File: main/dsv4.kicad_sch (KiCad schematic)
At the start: 2 parts, among them J101 Conn_01x02, J102 Conn_01x02

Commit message: Update, with FTDI, mostly OK
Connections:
- no-connect marks 0 -> 6
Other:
- added sheet MOT B Connection (mot_connector.kicad_sch)
- sheet MCU ports: added SPI_~{CS}_1, SPI_~{CS}_2, USART{UART}; removed none
- sheet MOT A Connection ports: added COD_PWM, COD_U, COD_V, COD{ENC}, MOT{MOT}, SPI_CSN, SPI{SPI}; removed none
- sheet Radio and misc ports: added UART{UART}; removed none

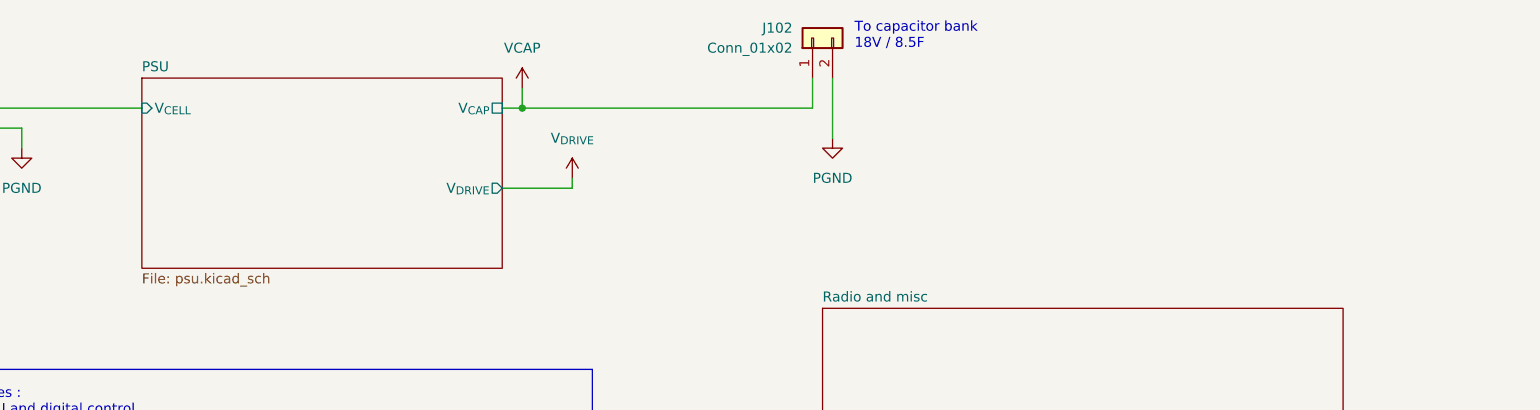
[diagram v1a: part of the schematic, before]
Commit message: Finalize schema for bat charger
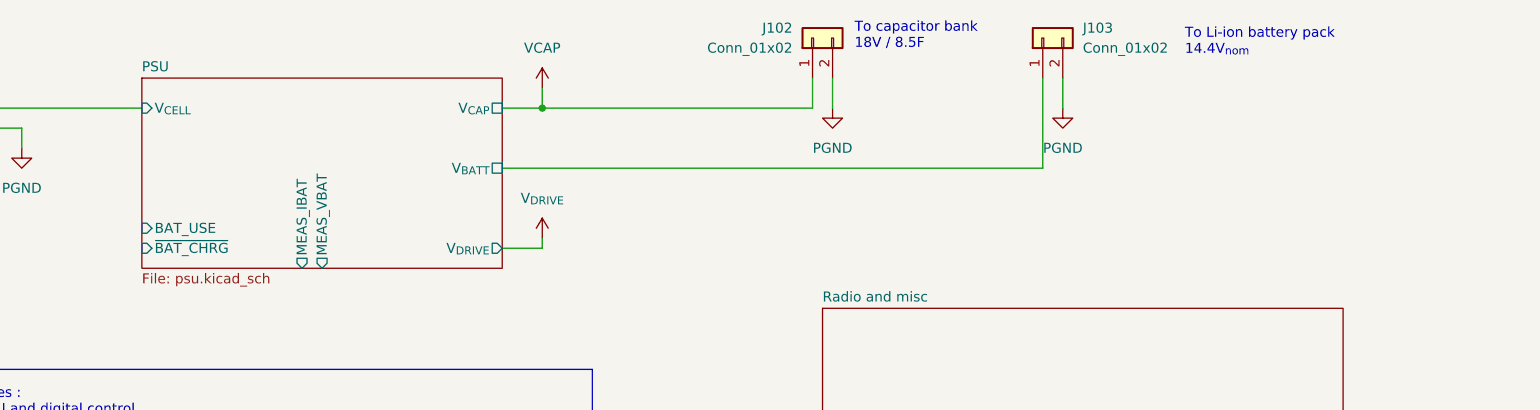
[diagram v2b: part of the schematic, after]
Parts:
- added J103: Conn_01x02, symbol Connector_Generic:Conn_01x02
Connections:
- net PGND: now also J103.2 (Pin_2)
- new net PSU/V_{BATT}: J103.1 (Pin_1)
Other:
- sheet PSU ports: added BAT_USE, MEAS_IBAT, MEAS_VBAT, V_{BATT}, ~{BAT_CHRG}; removed none
- note added: "To Li-ion battery pack 14.4V_{nom}"

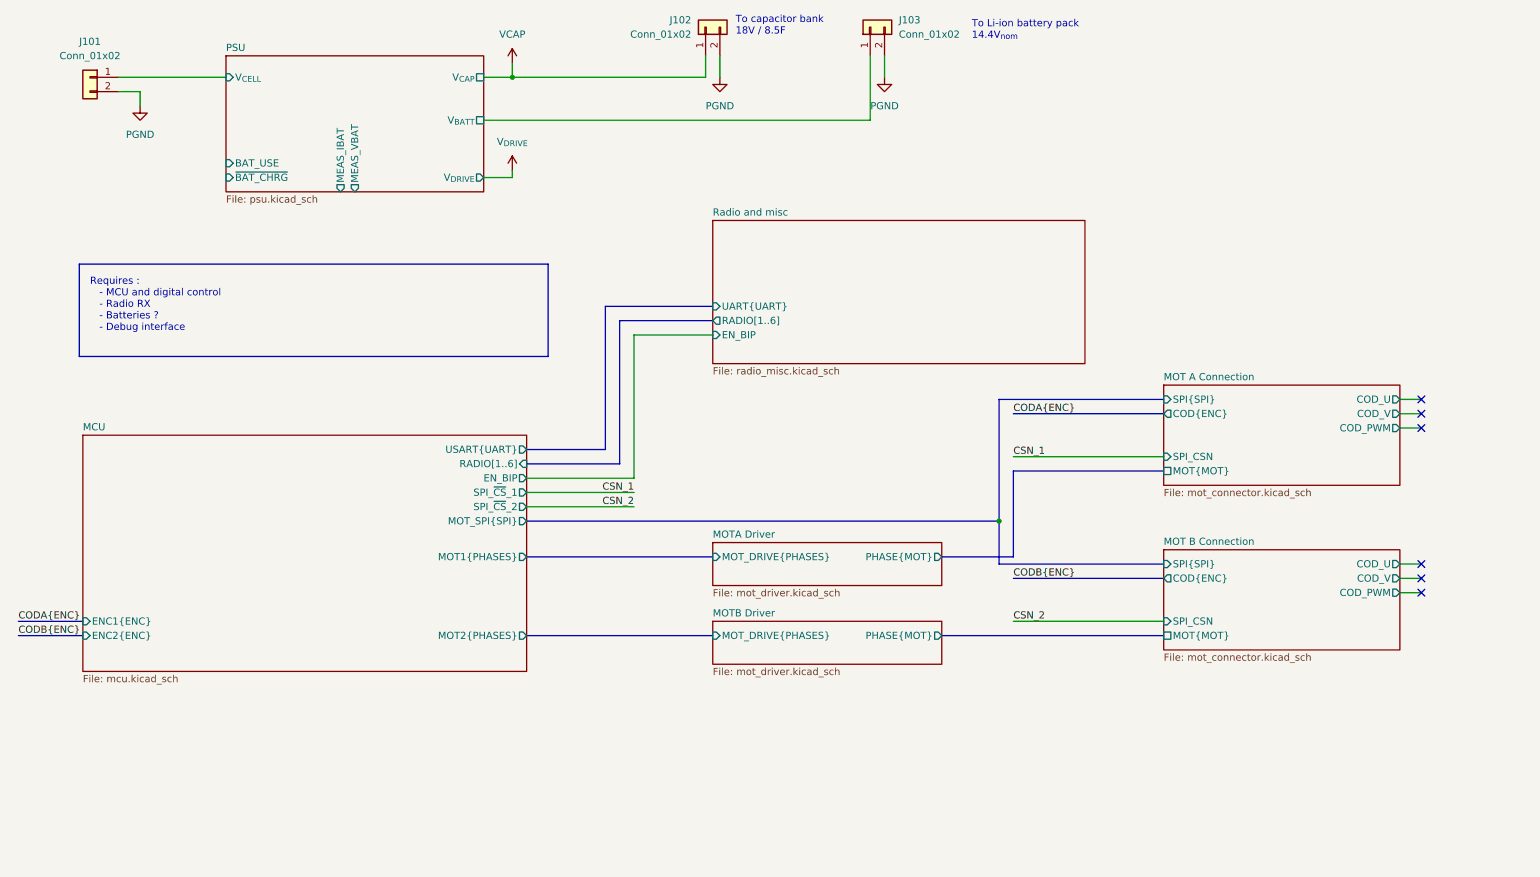
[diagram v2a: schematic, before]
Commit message: Finalize sch and start component mapping
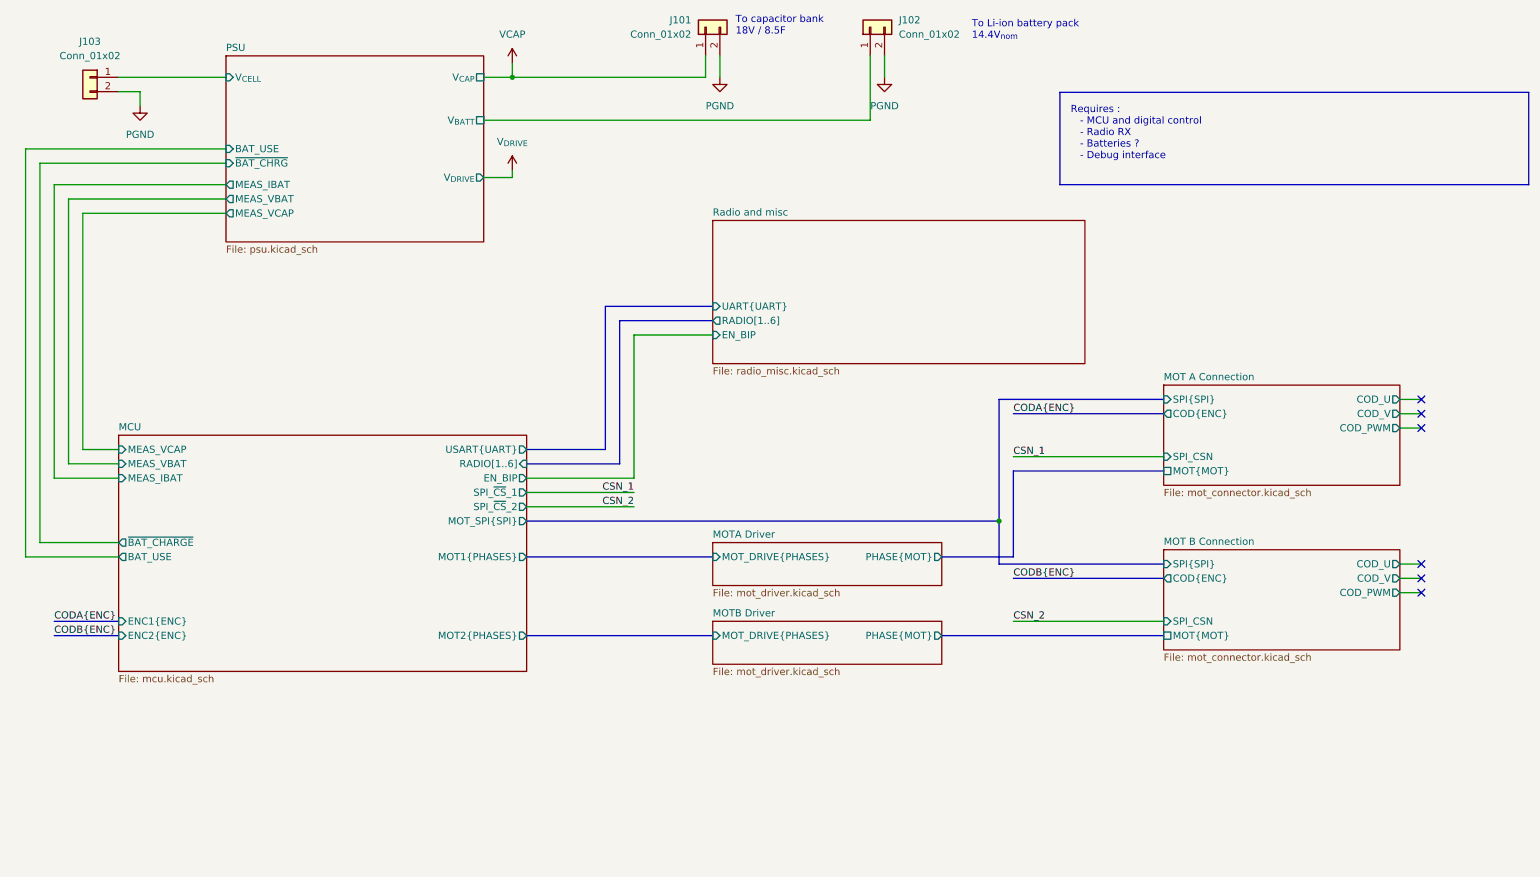
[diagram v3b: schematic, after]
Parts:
- renumbered J102 to J101, J103 to J102, J101 to J103
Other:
- sheet MCU ports: added BAT_USE, MEAS_IBAT, MEAS_VBAT, MEAS_VCAP, ~{BAT_CHARGE}; removed none
- sheet PSU ports: added MEAS_VCAP; removed none
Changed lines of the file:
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@@
+	(wire
+		(pts
+			(xy 17.78 110.49) (xy 17.78 43.18)
+		)
+		(stroke
+			(width 0)
+			(type default)
+		)
+	)
 	(wire
 		(pts
@@
 		)
 	)
+	(wire
+		(pts
+			(xy 25.4 93.98) (xy 25.4 52.07)
+		)
+		(stroke
+			(width 0)
+			(type default)
+		)
+	)
 	(bus
 		(pts
@@
 	(bus
 		(pts
-			(xy 13.97 127) (xy 25.4 127)
+			(xy 20.32 127) (xy 31.75 127)
 		)
 		(stroke
@@
 	(wire
 		(pts
+			(xy 17.78 43.18) (xy 50.8 43.18)
+		)
+		(stroke
+			(width 0)
+			(type default)
+		)
+	)
+	(wire
+		(pts
 			(xy 96.52 27.94) (xy 101.6 27.94)
 		)
@@
 	(wire
 		(pts
+			(xy 15.24 40.64) (xy 15.24 113.03)
+		)
+		(stroke
+			(width 0)
+			(type default)
+		)
+	)
+	(wire
+		(pts
 			(xy 190.5 124.46) (xy 217.17 124.46)
 		)
@@
 		)
 	)
+	(wire
+		(pts
+			(xy 20.32 46.99) (xy 20.32 99.06)
+		)
+		(stroke
+			(width 0)
+			(type default)
+		)
+	)
 	(bus
 		(pts
@@
 	(bus
 		(pts
-			(xy 13.97 124.46) (xy 25.4 124.46)
+			(xy 20.32 124.46) (xy 31.75 124.46)
 		)
 		(stroke
@@
 	(wire
 		(pts
+			(xy 50.8 46.99) (xy 20.32 46.99)
+		)
+		(stroke
+			(width 0)
+			(type default)
+		)
+	)
+	(wire
+		(pts
 			(xy 104.14 104.14) (xy 123.19 104.14)
 		)
@@
 	(wire
 		(pts
+			(xy 22.86 49.53) (xy 22.86 96.52)
+		)
+		(stroke
+			(width 0)
+			(type default)
+		)
+	)
+	(wire
+		(pts
 			(xy 123.19 99.06) (xy 104.14 99.06)
 		)
@@
 		)
 	)
+	(wire
+		(pts
+			(xy 50.8 40.64) (xy 15.24 40.64)
+		)
+		(stroke
+			(width 0)
+			(type default)
+		)
+	)
 	(bus
 		(pts
@@
 	(wire
 		(pts
+			(xy 50.8 49.53) (xy 22.86 49.53)
+		)
+		(stroke
+			(width 0)
+			(type default)
+		)
+	)
+	(wire
+		(pts
 			(xy 96.52 35.56) (xy 165.1 35.56)
 		)
@@
 		)
 	)
+	(wire
+		(pts
+			(xy 15.24 113.03) (xy 31.75 113.03)
+		)
+		(stroke
+			(width 0)
+			(type default)
+		)
+	)
+	(wire
+		(pts
+			(xy 31.75 93.98) (xy 25.4 93.98)
+		)
+		(stroke
+			(width 0)
+			(type default)
+		)
+	)
+	(wire
+		(pts
+			(xy 20.32 99.06) (xy 31.75 99.06)
+		)
+		(stroke
+			(width 0)
+			(type default)
+		)
+	)
 	(bus
 		(pts
@@
 		)
 	)
+	(wire
+		(pts
+			(xy 31.75 110.49) (xy 17.78 110.49)
+		)
+		(stroke
+			(width 0)
+			(type default)
+		)
+	)
 	(bus
 		(pts
@@
 	(wire
 		(pts
+			(xy 22.86 96.52) (xy 31.75 96.52)
+		)
+		(stroke
+			(width 0)
+			(type default)
+		)
+	)
+	(wire
+		(pts
 			(xy 167.64 24.13) (xy 167.64 27.94)
 		)
@@
 		)
 	)
+	(wire
+		(pts
+			(xy 25.4 52.07) (xy 50.8 52.07)
+		)
+		(stroke
+			(width 0)
+			(type default)
+		)
+	)
 	(rectangle
-		(start 24.765 61.087)
-		(end 107.95 77.47)
+		(start 198.755 30.607)
+		(end 281.94 46.99)
 		(stroke
 			(width 0)
@@
 	(text "Requires :\n   - MCU and digital control\n   - Radio RX\n   - Batteries ?\n   - Debug interface"
 		(exclude_from_sim no)
-		(at 26.67 63.5 0)
+		(at 200.66 33.02 0)
 		(effects
 			(font
@@
 	)
 	(label "CODB{ENC}"
-		(at 13.97 127 0)
+		(at 20.32 127 0)
 		(fields_autoplaced yes)
 		(effects
@@
 	)
 	(label "CODA{ENC}"
-		(at 13.97 124.46 0)
+		(at 20.32 124.46 0)
 		(fields_autoplaced yes)
 		(effects
@@
 		(dnp no)
 		(fields_autoplaced yes)
-		(property "Reference" "#PWR0105"
+		(property "Reference" "#PWR0103"
 			(at 167.64 34.29 0)
 			(effects
@@
 			(project "dsv4"
 				(path "/c07e9297-fde8-4755-803e-d05072cd6096"
-					(reference "#PWR0105")
+					(reference "#PWR0103")
 					(unit 1)
 				)
@@
 		(dnp no)
 		(fields_autoplaced yes)
-		(property "Reference" "#PWR0103"
+		(property "Reference" "#PWR0101"
 			(at 101.6 29.21 0)
 			(effects
@@
 			(project "dsv4"
 				(path "/c07e9297-fde8-4755-803e-d05072cd6096"
-					(reference "#PWR0103")
+					(reference "#PWR0101")
 					(unit 1)
 				)
@@
 		(dnp no)
 		(fields_autoplaced yes)
-		(property "Reference" "J101"
+		(property "Reference" "J103"
 			(at 26.67 21.59 0)
 			(effects
@@
 			(project "dsv4"
 				(path "/c07e9297-fde8-4755-803e-d05072cd6096"
-					(reference "J101")
+					(reference "J103")
 					(unit 1)
 				)
@@
 		(on_board yes)
 		(dnp no)
-		(property "Reference" "J102"
+		(property "Reference" "J101"
 			(at 133.35 17.7799 90)
 			(effects
@@
 			(project "dsv4"
 				(path "/c07e9297-fde8-4755-803e-d05072cd6096"
-					(reference "J102")
+					(reference "J101")
 					(unit 1)
 				)
@@
 		(dnp no)
 		(fields_autoplaced yes)
-		(property "Reference" "J103"
+		(property "Reference" "J102"
 			(at 170.18 17.7799 90)
 			(effects
@@
 			(project "dsv4"
 				(path "/c07e9297-fde8-4755-803e-d05072cd6096"
-					(reference "J103")
+					(reference "J102")
 					(unit 1)
 				)
@@
 		(dnp no)
 		(fields_autoplaced yes)
-		(property "Reference" "#PWR0104"
+		(property "Reference" "#PWR0105"
 			(at 101.6 48.26 0)
 			(effects
@@
 			(project "dsv4"
 				(path "/c07e9297-fde8-4755-803e-d05072cd6096"
-					(reference "#PWR0104")
+					(reference "#PWR0105")
 					(unit 1)
 				)
@@
 		(dnp no)
 		(fields_autoplaced yes)
-		(property "Reference" "#PWR0101"
+		(property "Reference" "#PWR0104"
 			(at 35.56 39.37 0)
 			(effects
@@
 			(project "dsv4"
 				(path "/c07e9297-fde8-4755-803e-d05072cd6096"
-					(reference "#PWR0101")
+					(reference "#PWR0104")
 					(unit 1)
 				)
@@
 	)
 	(sheet
-		(at 25.4 91.44)
-		(size 78.74 41.91)
+		(at 31.75 91.44)
+		(size 72.39 41.91)
 		(fields_autoplaced yes)
 		(stroke
@@
 		)
 		(property "Sheetname" "MCU"
-			(at 25.4 90.7284 0)
+			(at 31.75 90.7284 0)
 			(effects
 				(font
@@
 		)
 		(property "Sheetfile" "mcu.kicad_sch"
-			(at 25.4 133.9346 0)
+			(at 31.75 133.9346 0)
 			(effects
 				(font
@@
 		)
 		(pin "ENC1{ENC}" input
-			(at 25.4 124.46 180)
+			(at 31.75 124.46 180)
 			(effects
 				(font
@@
 		)
 		(pin "ENC2{ENC}" input
-			(at 25.4 127 180)
+			(at 31.75 127 180)
 			(effects
 				(font
@@
 				)
 				(justify right)
+			)
+		)
+		(pin "MEAS_VCAP" input
+			(at 31.75 93.98 180)
+			(effects
+				(font
+					(size 1.27 1.27)
+				)
+				(justify left)
+			)
+		)
+		(pin "BAT_USE" output
+			(at 31.75 113.03 180)
+			(effects
+				(font
+					(size 1.27 1.27)
+				)
+				(justify left)
+			)
+		)
+		(pin "MEAS_VBAT" input
+			(at 31.75 96.52 180)
+			(effects
+				(font
+					(size 1.27 1.27)
+				)
+				(justify left)
+			)
+		)
+		(pin "MEAS_IBAT" input
+			(at 31.75 99.06 180)
+			(effects
+				(font
+					(size 1.27 1.27)
+				)
+				(justify left)
+			)
+		)
+		(pin "~{BAT_CHARGE}" output
+			(at 31.75 110.49 180)
+			(effects
+				(font
+					(size 1.27 1.27)
+				)
+				(justify left)
 			)
 		)
@@
 	(sheet
 		(at 50.8 24.13)
-		(size 45.72 24.13)
+		(size 45.72 33.02)
 		(fields_autoplaced yes)
 		(stroke
@@
 		)
 		(property "Sheetfile" "psu.kicad_sch"
-			(at 50.8 48.8446 0)
+			(at 50.8 57.7346 0)
 			(effects
 				(font
@@
 		)
 		(pin "~{BAT_CHRG}" input
-			(at 50.8 45.72 180)
+			(at 50.8 43.18 180)
 			(effects
 				(font
@@
 		)
 		(pin "BAT_USE" input
-			(at 50.8 43.18 180)
+			(at 50.8 40.64 180)
 			(effects
 				(font
@@
 		)
 		(pin "MEAS_IBAT" output
-			(at 71.12 48.26 270)
+			(at 50.8 46.99 180)
 			(effects
 				(font
@@
 		)
 		(pin "MEAS_VBAT" output
-			(at 73.66 48.26 270)
-			(effects
-				(font
+			(at 50.8 49.53 180)
+			(effects
+				(font
+					(size 1.27 1.27)
+				)
+				(justify left)
+			)
+		)
+		(pin "MEAS_VCAP" output
+			(at 50.8 52.07 180)
+			(effects
+				(font

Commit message: update BOM
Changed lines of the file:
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@@
-		(color 0 0 0 0)
-	)
-	(junction
-		(at 187.96 106.68)
-		(diameter 0)
 		(color 0 0 0 0)
 	)
@@
 	(bus
 		(pts
-			(xy 187.96 85.09) (xy 217.17 85.09)
+			(xy 190.5 85.09) (xy 217.17 85.09)
+		)
+		(stroke
+			(width 0)
+			(type default)
+		)
+	)
+	(bus
+		(pts
+			(xy 104.14 106.68) (xy 123.19 106.68)
 		)
 		(stroke
@@
 	(bus
 		(pts
-			(xy 187.96 114.3) (xy 217.17 114.3)
+			(xy 190.5 114.3) (xy 217.17 114.3)
 		)
 		(stroke
@@
 	(bus
 		(pts
-			(xy 190.5 97.79) (xy 217.17 97.79)
+			(xy 182.88 97.79) (xy 217.17 97.79)
 		)
 		(stroke
@@
 	(bus
 		(pts
-			(xy 187.96 106.68) (xy 187.96 114.3)
-		)
-		(stroke
-			(width 0)
-			(type default)
-		)
-	)
-	(bus
-		(pts
 			(xy 104.14 113.03) (xy 137.16 113.03)
 		)
@@
 		)
 	)
-	(bus
-		(pts
-			(xy 104.14 106.68) (xy 187.96 106.68)
-		)
-		(stroke
-			(width 0)
-			(type default)
-		)
-	)
 	(wire
 		(pts
@@
 	(bus
 		(pts
-			(xy 177.8 113.03) (xy 190.5 113.03)
+			(xy 177.8 113.03) (xy 182.88 113.03)
 		)
 		(stroke
@@
 	(bus
 		(pts
-			(xy 187.96 85.09) (xy 187.96 106.68)
-		)
-		(stroke
-			(width 0)
-			(type default)
-		)
-	)
-	(bus
-		(pts
-			(xy 190.5 113.03) (xy 190.5 97.79)
+			(xy 182.88 113.03) (xy 182.88 97.79)
 		)
 		(stroke
@@
 		)
 	)
+	(label "SPI{SPI}"
+		(at 190.5 85.09 0)
+		(fields_autoplaced yes)
+		(effects
+			(font
+				(size 1.27 1.27)
+			)
+			(justify left bottom)
+		)
+	)
 	(label "CODB{ENC}"
 		(at 20.32 127 0)
@@
 		)
 	)
+	(label "SPI{SPI}"
+		(at 190.5 114.3 0)
+		(fields_autoplaced yes)
+		(effects
+			(font
+				(size 1.27 1.27)
+			)
+			(justify left bottom)
+		)
+	)
 	(label "CSN_1"
 		(at 190.5 95.25 0)
@@
 		)
 	)
+	(label "SPI{SPI}"
+		(at 123.19 106.68 180)
+		(fields_autoplaced yes)
+		(effects
+			(font
+				(size 1.27 1.27)
+			)
+			(justify right bottom)
+		)
+	)

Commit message: BOM OK
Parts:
- J101, J102, J103: footprint (none) -> TerminalBlock_WAGO:TerminalBlock_WAGO_236-402_1x02_P5.00mm_45Degree
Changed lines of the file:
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@@
 			)
 		)
-		(property "Footprint" ""
+		(property "Footprint" "TerminalBlock_WAGO:TerminalBlock_WAGO_236-402_1x02_P5.00mm_45Degree"
 			(at 26.67 27.94 0)
 			(effects
@@
 			)
 		)
-		(property "Footprint" ""
+		(property "Footprint" "TerminalBlock_WAGO:TerminalBlock_WAGO_236-402_1x02_P5.00mm_45Degree"
 			(at 135.89 19.05 0)
 			(effects
@@
 			)
 		)
-		(property "Footprint" ""
+		(property "Footprint" "TerminalBlock_WAGO:TerminalBlock_WAGO_236-402_1x02_P5.00mm_45Degree"
 			(at 165.1 19.05 0)
 			(effects

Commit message: Update PCB
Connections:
- net PGND: now also J101.1 (Pin_1); no longer J101.2 (Pin_2)
- net VCAP: now also J101.2 (Pin_2); no longer J101.1 (Pin_1)
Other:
- moved on the sheet: J101
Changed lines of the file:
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@@
 		(on_board yes)
 		(dnp no)
-		(fields_autoplaced yes)
 		(property "Reference" "J103"
 			(at 26.67 21.59 0)
@@
 	(symbol
 		(lib_id "Connector_Generic:Conn_01x02")
-		(at 135.89 19.05 90)
+		(at 138.43 19.05 270)
+		(mirror x)
 		(unit 1)
 		(exclude_from_sim no)
@@
 		(on_board yes)
 		(dnp no)
+		(fields_autoplaced yes)
 		(property "Reference" "J101"
 			(at 133.35 17.7799 90)
@@
 					(size 1.27 1.27)
 				)
-				(justify left)
+				(justify right)
 			)
 		)
@@
 					(size 1.27 1.27)
 				)
-				(justify left)
+				(justify right)
 			)
 		)
 		(property "Footprint" "TerminalBlock_WAGO:TerminalBlock_WAGO_236-402_1x02_P5.00mm_45Degree"
-			(at 135.89 19.05 0)
+			(at 138.43 19.05 0)
 			(effects
 				(font
@@
 		)
 		(property "Datasheet" "~"
-			(at 135.89 19.05 0)
+			(at 138.43 19.05 0)
 			(effects
 				(font
@@
 		)
 		(property "Description" "Generic connector, single row, 01x02, script generated (kicad-library-utils/schlib/autogen/connector/)"
-			(at 135.89 19.05 0)
+			(at 138.43 19.05 0)
 			(effects
 				(font

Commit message: Route of power rails
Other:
- sheet MCU ports: added BAT_OK; removed none
- sheet PSU ports: added BATT_OK; removed none
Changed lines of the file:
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@@
+	(wire
+		(pts
+			(xy 50.8 38.1) (xy 12.7 38.1)
+		)
+		(stroke
+			(width 0)
+			(type default)
+		)
+	)
 	(wire
 		(pts
@@
 	(wire
 		(pts
+			(xy 12.7 115.57) (xy 31.75 115.57)
+		)
+		(stroke
+			(width 0)
+			(type default)
+		)
+	)
+	(wire
+		(pts
 			(xy 50.8 46.99) (xy 20.32 46.99)
 		)
@@
 	(wire
 		(pts
+			(xy 12.7 38.1) (xy 12.7 115.57)
+		)
+		(stroke
+			(width 0)
+			(type default)
+		)
+	)
+	(wire
+		(pts
 			(xy 31.75 110.49) (xy 17.78 110.49)
 		)
@@
 	(wire
 		(pts
-			(xy 35.56 33.02) (xy 35.56 30.48)
+			(xy 35.56 31.75) (xy 35.56 30.48)
 		)
 		(stroke
@@
 	(symbol
 		(lib_id "power:GND")
-		(at 35.56 33.02 0)
+		(at 35.56 31.75 0)
 		(unit 1)
 		(exclude_from_sim no)
@@
 		(fields_autoplaced yes)
 		(property "Reference" "#PWR0104"
-			(at 35.56 39.37 0)
+			(at 35.56 38.1 0)
 			(effects
 				(font
@@
 		)
 		(property "Value" "PGND"
-			(at 35.56 38.1 0)
+			(at 35.56 36.83 0)
 			(effects
 				(font
@@
 		)
 		(property "Footprint" ""
-			(at 35.56 33.02 0)
+			(at 35.56 31.75 0)
 			(effects
 				(font
@@
 		)
 		(property "Datasheet" ""
-			(at 35.56 33.02 0)
+			(at 35.56 31.75 0)
 			(effects
 				(font
@@
 		)
 		(property "Description" "Power symbol creates a global label with name \"GND\" , ground"
-			(at 35.56 33.02 0)
+			(at 35.56 31.75 0)
 			(effects
 				(font
@@
 			)
 		)
+		(pin "BAT_OK" input
+			(at 31.75 115.57 180)
+			(effects
+				(font
+					(size 1.27 1.27)
+				)
+				(justify left)
+			)
+		)
 		(instances
 			(project "dsv4"
@@
 			(effects
 				(font
+					(size 1.27 1.27)
+				)
+				(justify left)
+			)
+		)
+		(pin "BATT_OK" output
+			(at 50.8 38.1 180)
+			(effects
+				(font
